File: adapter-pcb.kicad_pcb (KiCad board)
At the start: 4 copper layers, 90.2 x 95.9 mm, 22 parts, among them J1 SS5-80-3.50-X-D-K-XX, J2 DM3BT-DSF-PEJS, U2 LTC4300A-1IMS8_PBF

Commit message: Made some minor adjustments
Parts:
- C27: footprint Capacitor_SMD:C_0402_1005Metric -> Capacitor_SMD:C_0603_1608Metric
- C33: footprint Capacitor_SMD:C_0402_1005Metric -> Capacitor_SMD:C_0805_2012Metric
- moved C33 7.99 mm to (167.9, 87.8), turned to 90 degrees
- moved C27 7.21 mm to (169.7, 87.8), turned to 90 degrees
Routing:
- net +3V3: track 29.3 -> 188.8 mm, vias 11 -> 5
- net I2C_SDA_CSKB: track 66.3 -> 99.8 mm, vias 2 -> 0
- net I2C_SCL_CSKB: track 73.3 -> 95.1 mm, vias 4 -> 0
- net MOSI: track 38.0 -> 58.1 mm, vias 1 -> 0
- net SNN Enable: track 93.5 -> 106.8 mm, vias 2 -> 0
- net SS/CS: track 43.5 -> 56.0 mm, vias 1 -> 0
- net RESESTREQ: track 93.5 -> 103.4 mm, vias 2 -> 0
- net SD-CCLK: track 36.8 -> 46.1 mm
- net UART_TX: track 63.3 -> 54.0 mm, vias 2 -> 0
- net SD-D1: track 37.8 -> 45.9 mm, vias 2 -> 0
- net SD-D2: track 39.8 -> 45.9 mm, vias 1 -> 0
- net SD-CMD: track 37.5 -> 43.0 mm, vias 0 -> 2
- net GND: track 47.9 -> 53.3 mm, vias 51 -> 86
- net UART_RX: track 54.4 -> 49.9 mm, vias 2 -> 0
- net SCLK: track 60.8 -> 56.5 mm
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- removed copper zone on In2.Cu, net +3V3
- removed copper zone on In1.Cu, net GND
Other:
- copper layers 4 -> 2

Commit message: fixed 3D models
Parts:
- J1: value SS5-80-3.50-X-D-K-XX -> SS5-80-3.50-L-D-K-TR

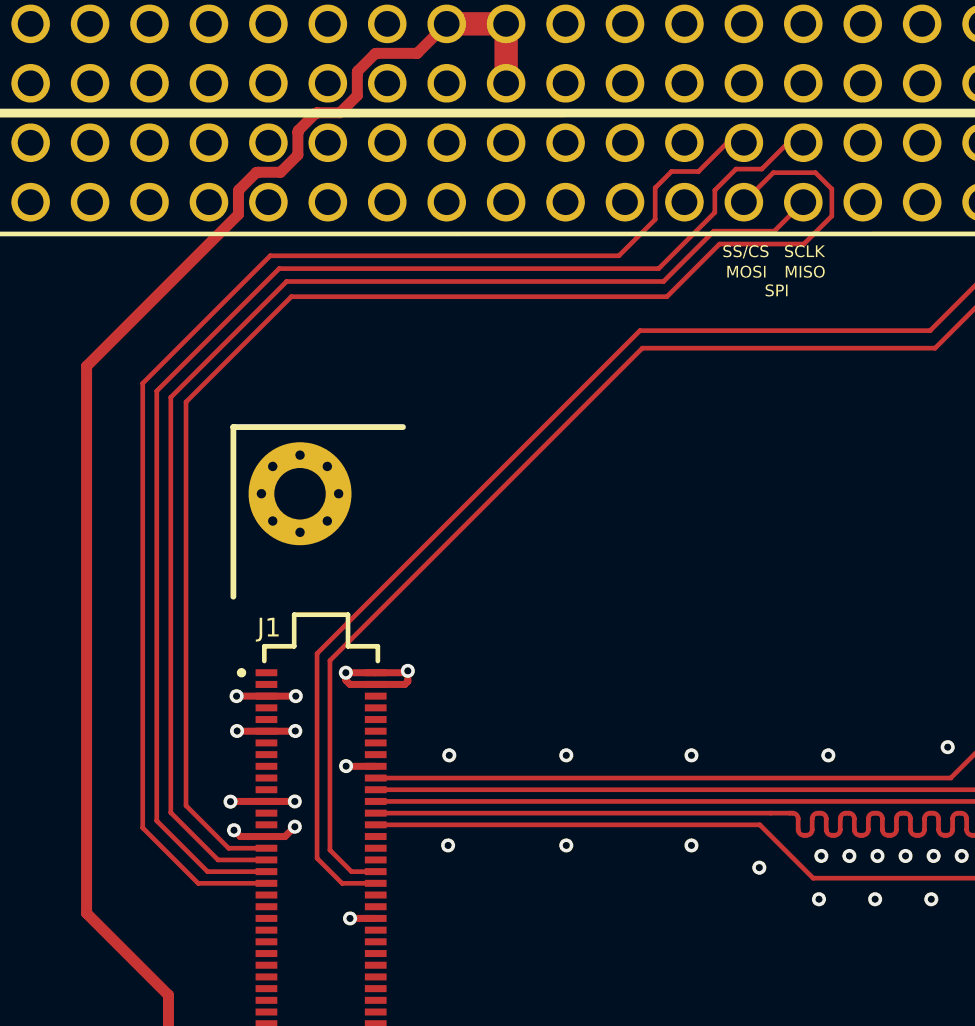
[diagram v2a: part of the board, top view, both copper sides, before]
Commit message: Removed SPI Connections
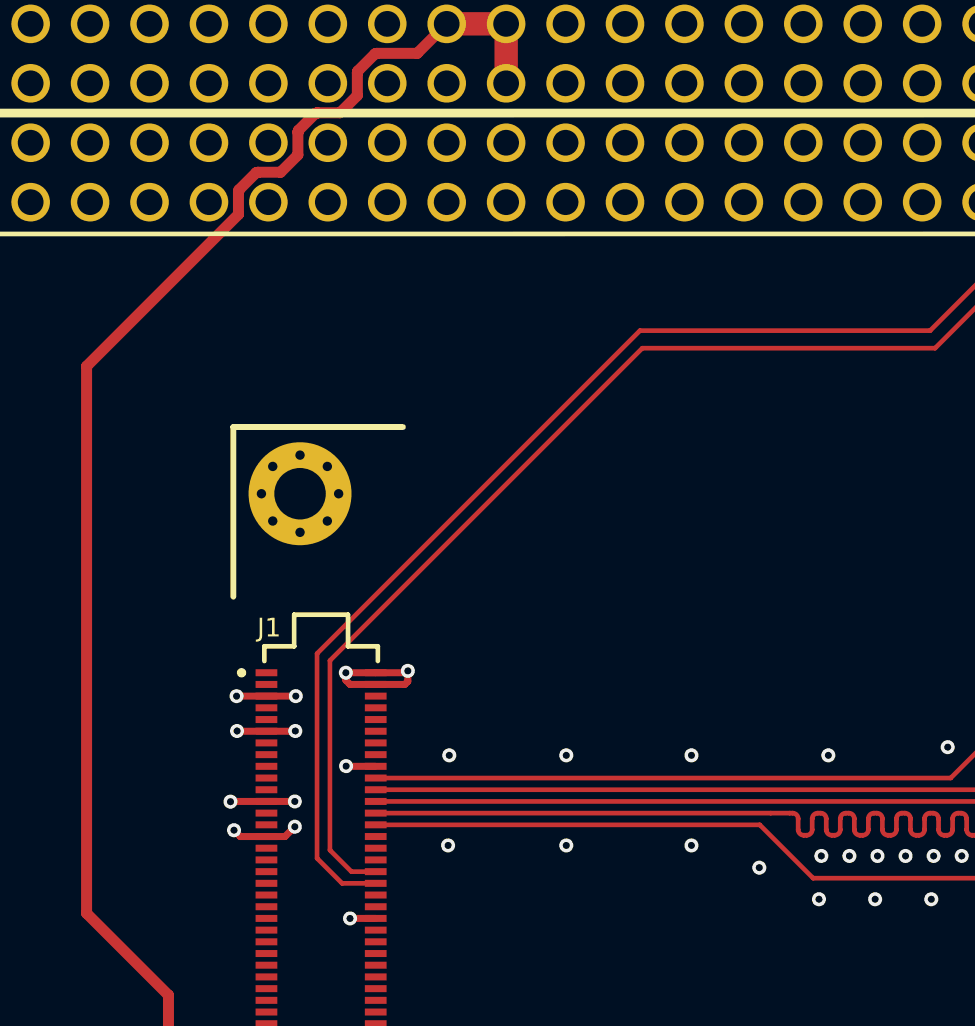
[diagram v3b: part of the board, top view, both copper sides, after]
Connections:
- H1 pad 27: MOSI -> unconnected-(H1-Pin_27-Pad27)
- H1 pad 28: SS/CS -> unconnected-(H1-Pin_28-Pad28)
- H1 pad 29: MISO -> unconnected-(H1-Pin_29-Pad29)
- H1 pad 30: SCLK -> unconnected-(H1-Pin_30-Pad30)
- J1 pad 31: MOSI -> unconnected-(J1A-MIO10-Pad31)
- J1 pad 33: MISO -> unconnected-(J1A-MIO11-Pad33)
- J1 pad 35: SCLK -> unconnected-(J1A-MIO12-Pad35)
- J1 pad 37: SS/CS -> unconnected-(J1A-MIO13-Pad37)
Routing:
- net MOSI: track 58.1 -> 0.00 mm
- net SCLK: track 56.5 -> 0.00 mm
- net SS/CS: track 56.0 -> 0.00 mm
- net MISO: track 53.2 -> 0.00 mm
- net unconnected-(H1-Pin_28-Pad28): track 0.00 -> 0.71 mm
- net unconnected-(H1-Pin_30-Pad30): track 0.00 -> 0.65 mm
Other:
- board text removed: "MISO"
- board text removed: "MOSI"
- board text removed: "SCLK"
- board text removed: "SPI"
- board text removed: "SS/CS"

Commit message: Added hierarchical lables to the schematic
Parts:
- added REF**: WEEE-Logo_5.6x8mm_SilkScreen, Symbol:WEEE-Logo_5.6x8mm_SilkScreen, B.Cu at (181.4, 127.4)
- added REF**: ESD-Logo_6.6x6mm_SilkScreen, Symbol:ESD-Logo_6.6x6mm_SilkScreen, B.Cu at (181.4, 118.4)
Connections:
- net I2C_SCL(2) renamed /I2C Buffer/I2C_SCL(2)
- net I2C_SCL_CSKB renamed /CSKB/I2C_SCL_CSKB
- net I2C_SDA(2) renamed /I2C Buffer/I2C_SDA(2)
- net I2C_SDA_CSKB renamed /CSKB/I2C_SDA_CSKB
- net RESESTREQ renamed /CSKB/RESESTREQ
- net SD-CCLK renamed /Micro SD/SD-CCLK
- net SD-CMD renamed /Micro SD/SD-CMD
- net SD-D0 renamed /Micro SD/SD-D0
- net SD-D1 renamed /Micro SD/SD-D1
- net SD-D2 renamed /Micro SD/SD-D2
- net SD-D3 renamed /TE0724 Connector/SD-D3
- net SNN Enable renamed /CSKB/ENABLE
- net UART_RX renamed /CSKB/UART_RX
- net UART_TX renamed /CSKB/UART_TX
